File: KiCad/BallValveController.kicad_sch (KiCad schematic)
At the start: 53 parts, among them J1 Screw_Terminal_01x03, J2 Screw_Terminal_01x04, J3 Screw_Terminal_01x04, J4 Screw_Terminal_01x04, J5 Conn_01x01_Male, J6 Screw_Terminal_01x04, J7 Screw_Terminal_01x02, K1 G5V-2, Q1 Q_PMOS_GDS, Q2 2N2222A, U1 MT2499A, U2 L7805, U3 XIAO-ESP32-C6

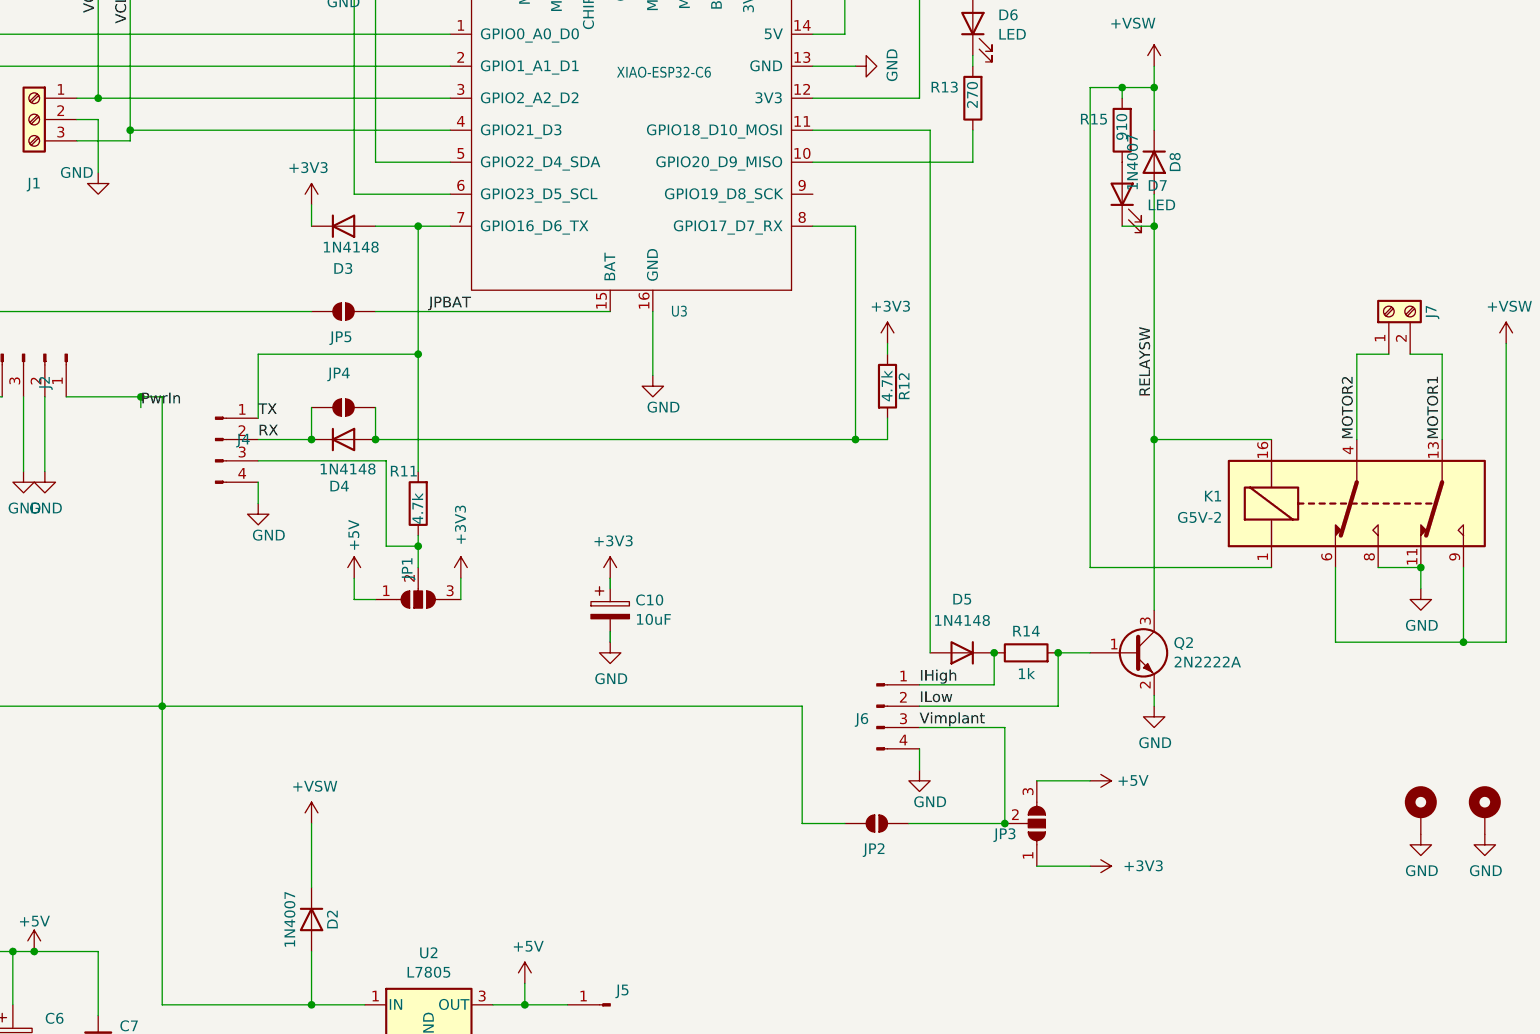
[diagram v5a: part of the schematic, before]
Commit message: New layout - changed Diodes and Cap footprints + RX/TX wiring
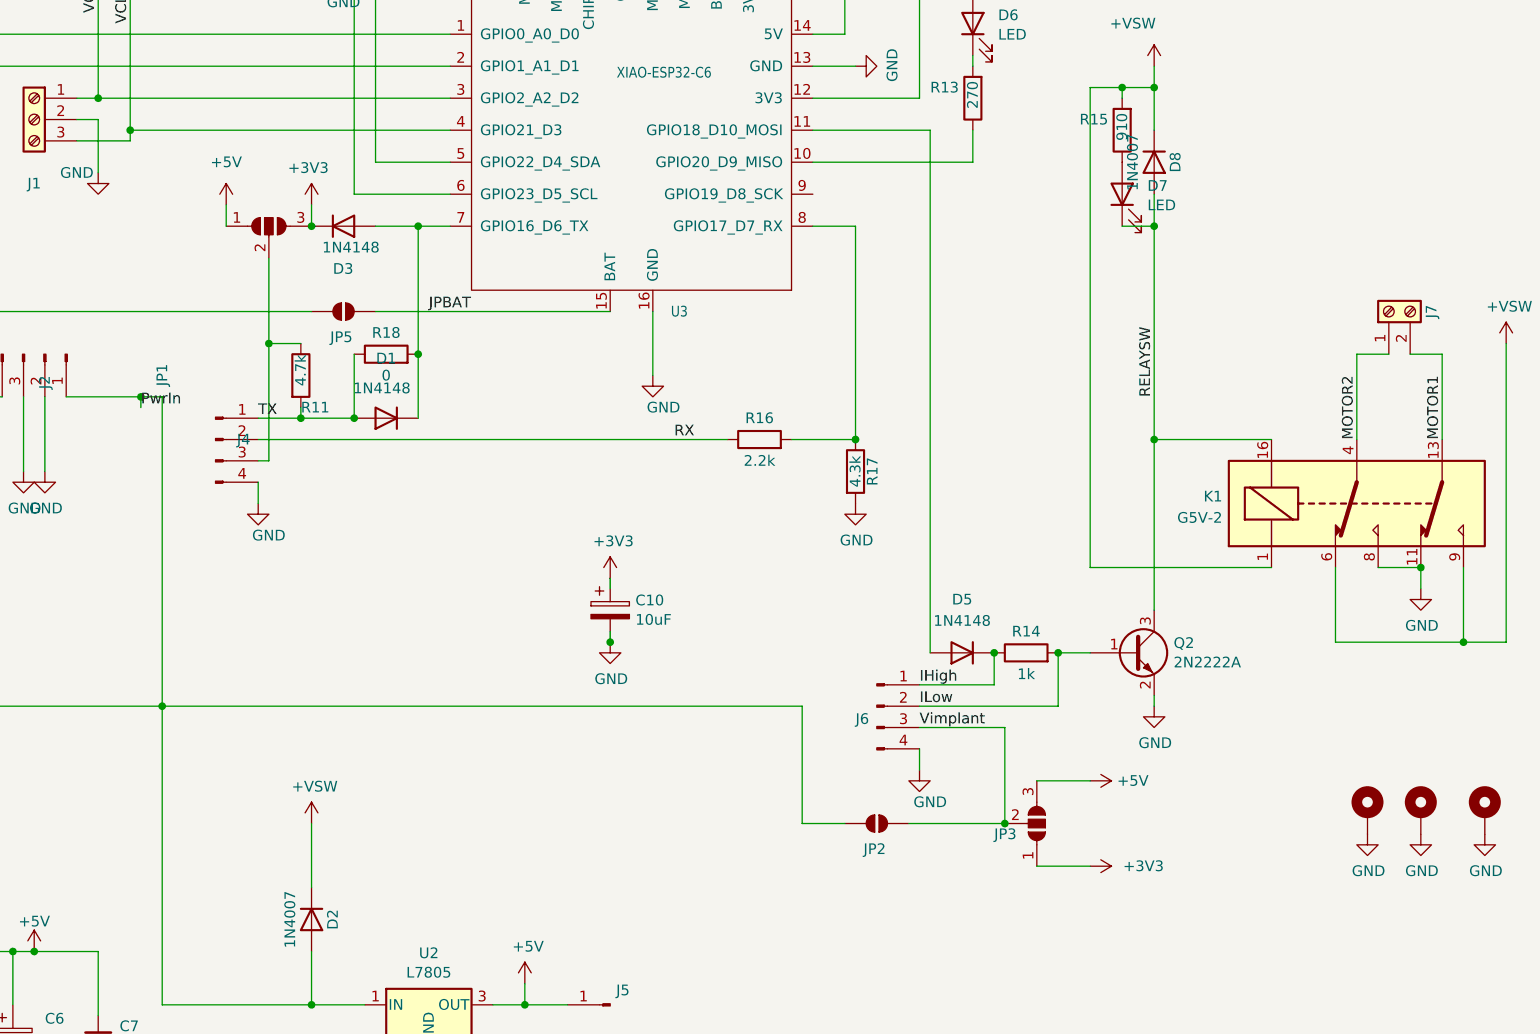
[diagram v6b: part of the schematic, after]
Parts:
- removed D4: 1N4148, Diode_SMD:D_SOD-323_HandSoldering, symbol Device:D
- removed JP4: SolderJumper_2_Open, Jumper:SolderJumper-2_P1.3mm_Open_RoundedPad1.0x1.5mm, symbol Jumper:SolderJumper_2_Open
- removed R12: 4.7k, Resistor_SMD:R_0805_2012Metric_Pad1.20x1.40mm_HandSolder, symbol Device:R
- added D1: 1N4148, Diode_SMD:D_SOD-323_HandSoldering, symbol Device:D
- added H2: MountingHole_Pad, MountingHole:MountingHole_3.2mm_M3_ISO14580_Pad, symbol Mechanical:MountingHole_Pad
- added R16: 2.2k, Resistor_SMD:R_0805_2012Metric_Pad1.20x1.40mm_HandSolder, symbol Device:R
- added R17: 4.3k, Resistor_SMD:R_0805_2012Metric_Pad1.20x1.40mm_HandSolder, symbol Device:R
- added R18: 0, Resistor_SMD:R_0805_2012Metric_Pad1.20x1.40mm_HandSolder, symbol Device:R
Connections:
- net GND: now also H2.1, R17.2
- net RX: now also R16.1
- net TX: now also D1.2 (A), R18.1; no longer D3.2 (A), U3.7 (GPIO16_D6_TX)
- net at U3.8 (GPIO17_D7_RX): now also R16.2, R17.1
- new net: D1.1 (K), D3.2 (A), R18.2, U3.7 (GPIO16_D6_TX)
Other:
- moved on the sheet: JP1, R11

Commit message: Version 8.0.2 pdf files
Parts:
- added TP1, TP2, TP3, TP4, TP5, TP6: TestPoint, TestPoint:TestPoint_THTPad_D1.0mm_Drill0.5mm, symbol Connector:TestPoint
- Q2: footprint Package_TO_SOT_SMD:SOT-23_Handsoldering -> Package_TO_SOT_SMD:SOT-23
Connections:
- net +3V3: now also TP3.1
- net +5V: now also TP2.1
- net +VSW: now also TP5.1
- net RELAYSW: now also TP4.1
- net VBAT: now also TP6.1
- net at C4.2, Q1.1 (G), R6.1: now also TP1.1
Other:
- title: Ball Valve Controller for CR05-02 wiring - ESP32-C3 version -> Ball Valve Controller for CR05-02 wiring - ESP32-C3/C6

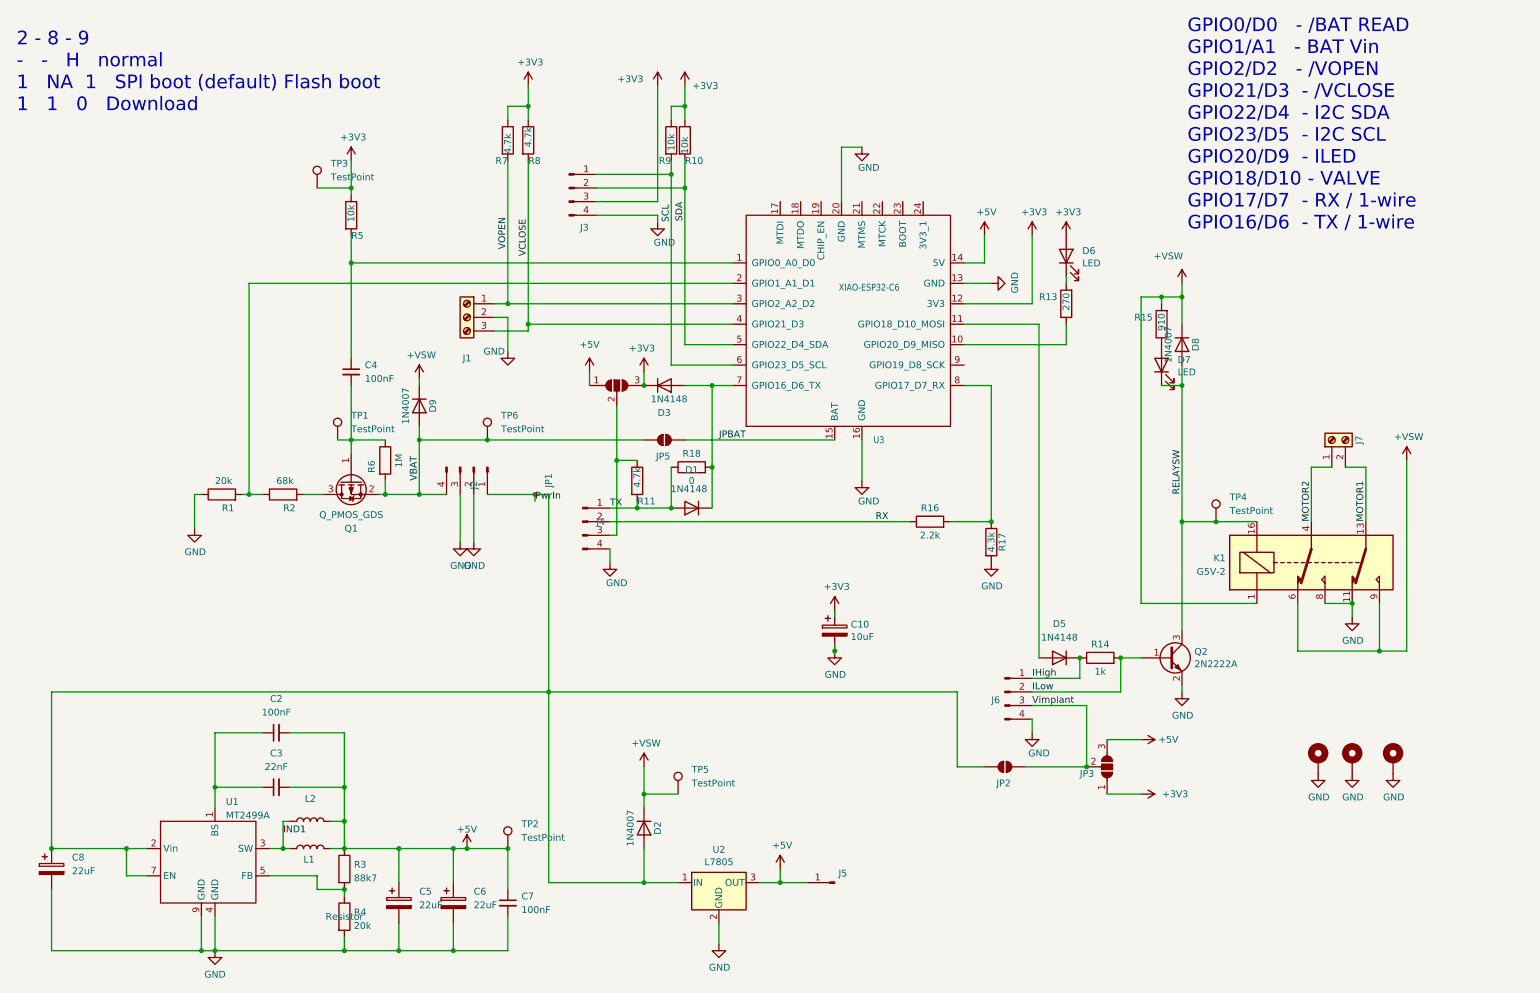
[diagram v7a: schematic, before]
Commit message: Fixed MT2499A layout
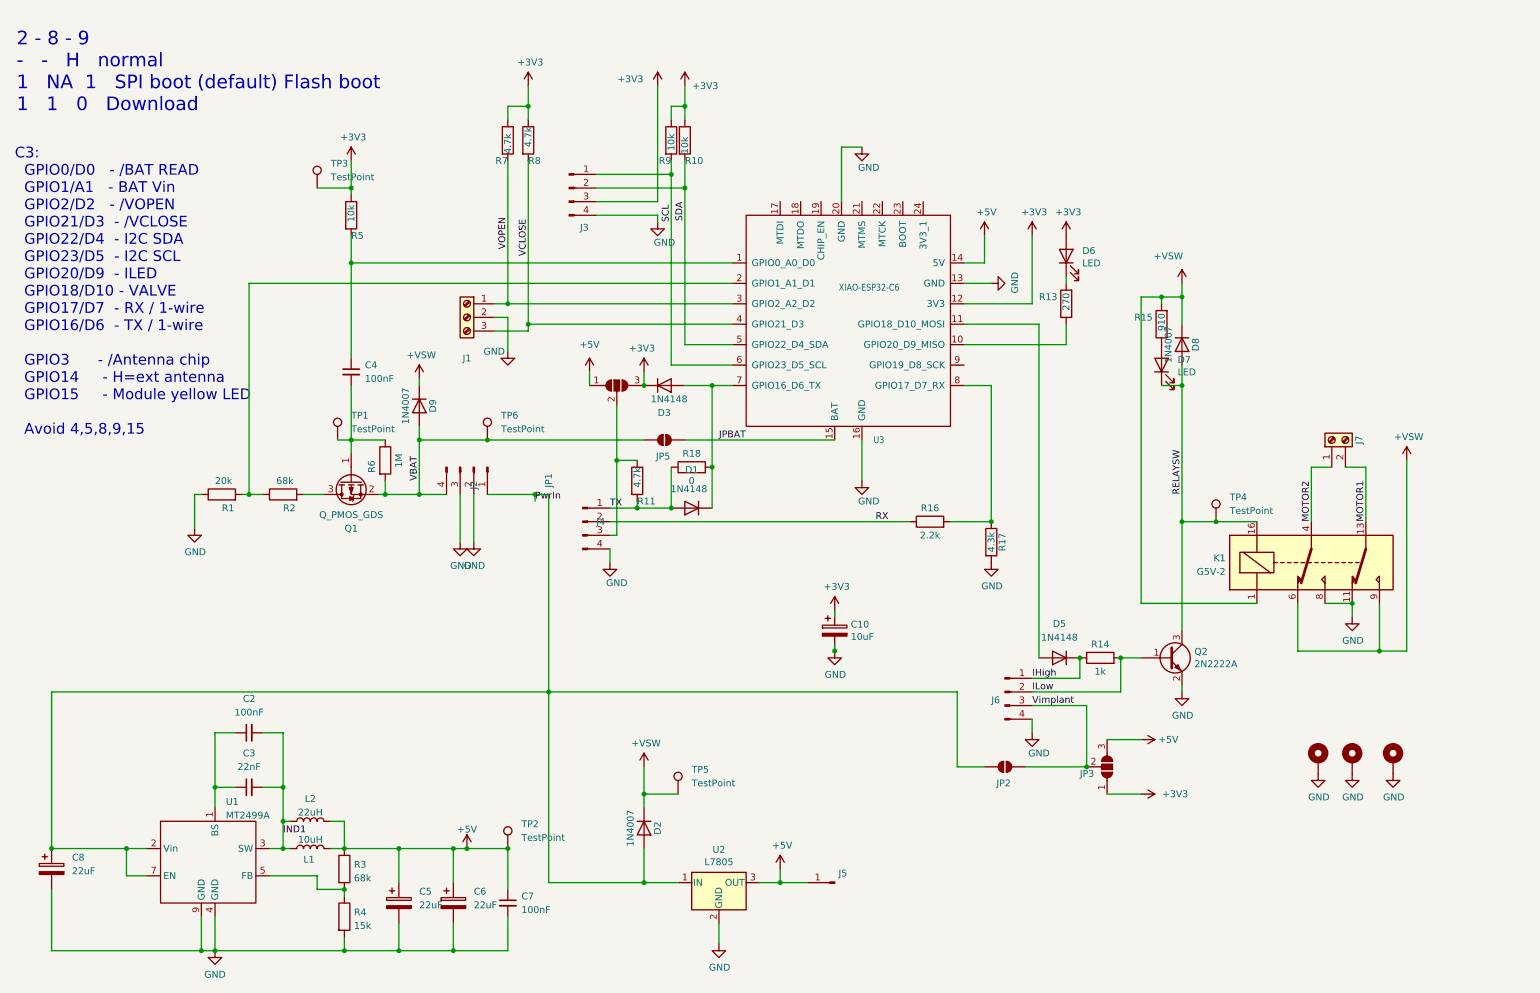
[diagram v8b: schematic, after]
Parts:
- L1: value L -> 10uH; footprint Inductor_SMD:L_2512_6332Metric_Pad1.52x3.35mm_HandSolder -> Inductor_SMD:L_2010_5025Metric_Pad1.52x2.65mm_HandSolder
- L2: value L -> 22uH
- R3: value 88k7 -> 68k
- R4: value 20k -> 15k
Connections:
- net +5V: no longer C2.2, C3.2
- net IND1: now also C2.2, C3.2
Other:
- note added: "C3: GPIO0/D0 - /BAT READ GPIO1/A1 - BAT Vin GPIO2/D2 - /VOPEN GPIO21/D3 - /VCLOSE GPIO22/D4 - I2C SDA GPIO23/D5 - I2C SCL GPIO20/D9 - ILED GPIO18/D10 - VALVE GPIO17/D7 - RX / 1-wire GPIO16/D6 - TX / 1-wire GPIO3 - /Antenna chip GPIO14 - H=ext antenna GPIO15 - Module yellow LED Avoid 4,5,8,9,15"
- note removed: "GPIO0/D0 - /BAT READ GPIO1/A1 - BAT Vin GPIO2/D2 - /VOPEN GPIO21/D3 - /VCLOSE GPIO22/D4 - I2C SDA GPIO23/D5 - I2C SCL GPIO20/D9 - ILED GPIO18/D10 - VALVE GPIO17/D7 - RX / 1-wire GPIO16/D6 - TX / 1-wire"
- moved on the sheet: C2, C3
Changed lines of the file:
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@@
 		)
 	)
-	(text "GPIO0/D0   - /BAT READ\nGPIO1/A1   - BAT Vin\nGPIO2/D2   - /VOPEN\nGPIO21/D3  - /VCLOSE\nGPIO22/D4  - I2C SDA\nGPIO23/D5  - I2C SCL\nGPIO20/D9  - ILED\nGPIO18/D10 - VALVE\nGPIO17/D7  - RX / 1-wire\nGPIO16/D6  - TX / 1-wire\n\n"
+	(text "C3:\n  GPIO0/D0   - /BAT READ\n  GPIO1/A1   - BAT Vin\n  GPIO2/D2   - /VOPEN\n  GPIO21/D3  - /VCLOSE\n  GPIO22/D4  - I2C SDA\n  GPIO23/D5  - I2C SCL\n  GPIO20/D9  - ILED\n  GPIO18/D10 - VALVE\n  GPIO17/D7  - RX / 1-wire\n  GPIO16/D6  - TX / 1-wire\n\n  GPIO3      - /Antenna chip\n  GPIO14     - H=ext antenna\n  GPIO15     - Module yellow LED\n\n  Avoid 4,5,8,9,15\n\n"
 		(exclude_from_sim no)
-		(at 233.426 59.182 0)
+		(at 14.732 96.52 0)
 		(effects
 			(font
 				(face "Andale Mono")
-				(size 2.54 2.54)
+				(size 2 2)
 			)
 			(justify left bottom)
@@
 	)
 	(junction
-		(at 232.41 109.22)
+		(at 64.77 165.1)
 		(diameter 0)
 		(color 0 0 0 0)
 	)
 	(junction
-		(at 111.76 104.14)
+		(at 232.41 109.22)
 		(diameter 0)
 		(color 0 0 0 0)
 	)
 	(junction
-		(at 213.36 134.62)
+		(at 111.76 104.14)
 		(diameter 0)
 		(color 0 0 0 0)
 	)
 	(junction
-		(at 232.41 67.31)
+		(at 213.36 134.62)
 		(diameter 0)
 		(color 0 0 0 0)
 	)
 	(junction
-		(at 76.2 158.75)
+		(at 232.41 67.31)
 		(diameter 0)
 		(color 0 0 0 0)
@@
 	)
 	(junction
+		(at 64.77 158.75)
+		(diameter 0)
+		(color 0 0 0 0)
+	)
+	(junction
 		(at 76.2 177.8)
 		(diameter 0)
@@
 	)
 	(junction
-		(at 76.2 165.1)
-		(diameter 0)
-		(color 0 0 0 0)
-	)
-	(junction
 		(at 58.42 104.14)
 		(diameter 0)
@@
 	(wire
 		(pts
-			(xy 52.07 148.59) (xy 60.96 148.59)
+			(xy 52.07 148.59) (xy 55.88 148.59)
 		)
 		(stroke
@@
 	(wire
 		(pts
-			(xy 66.04 148.59) (xy 76.2 148.59)
+			(xy 60.96 148.59) (xy 64.77 148.59)
 		)
 		(stroke
@@
 	(wire
 		(pts
-			(xy 52.07 158.75) (xy 60.96 158.75)
+			(xy 52.07 158.75) (xy 55.88 158.75)
 		)
 		(stroke
@@
 	(wire
 		(pts
-			(xy 66.04 158.75) (xy 76.2 158.75)
+			(xy 60.96 158.75) (xy 64.77 158.75)
 		)
 		(stroke
@@
 	(wire
 		(pts
-			(xy 76.2 148.59) (xy 76.2 158.75)
+			(xy 64.77 148.59) (xy 64.77 158.75)
 		)
 		(stroke
@@
 	(wire
 		(pts
-			(xy 76.2 158.75) (xy 76.2 165.1)
-		)
-		(stroke
-			(width 0)
-			(type default)
-		)
-	)
-	(wire
-		(pts
 			(xy 220.98 134.62) (xy 220.98 140.97)
 		)
@@
 	(wire
 		(pts
+			(xy 64.77 158.75) (xy 64.77 165.1)
+		)
+		(stroke
+			(width 0)
+			(type default)
+		)
+	)
+	(wire
+		(pts
 			(xy 123.19 44.45) (xy 137.16 44.45)
 		)
@@
 			)
 		)
-		(property "Value" "20k"
+		(property "Value" "15k"
 			(at 77.978 184.5822 0)
 			(effects
@@
 					(size 1.27 1.27)
 				)
+				(hide yes)
 			)
 		)
@@
 			)
 		)
-		(property "Value" "88k7"
+		(property "Value" "68k"
 			(at 77.978 175.6922 0)
 			(effects
@@
 			)
 		)
-		(property "Value" "L"
+		(property "Value" "10uH"
 			(at 69.85 168.5091 90)
 			(effects
@@
 					(size 1.27 1.27)
 				)
-				(hide yes)
 			)
 		)
-		(property "Footprint" "Inductor_SMD:L_2512_6332Metric_Pad1.52x3.35mm_HandSolder"
+		(property "Footprint" "Inductor_SMD:L_2010_5025Metric_Pad1.52x2.65mm_HandSolder"
 			(at 69.85 170.18 0)
 			(effects
@@
 	(symbol
 		(lib_id "Device:C_Small")
-		(at 63.5 148.59 90)
+		(at 58.42 148.59 90)
 		(unit 1)
 		(exclude_from_sim no)
@@
 		(fields_autoplaced yes)
 		(property "Reference" "C2"
-			(at 63.5063 142.24 90)
+			(at 58.4263 142.24 90)
 			(effects
 				(font
@@
 		)
 		(property "Value" "100nF"
-			(at 63.5063 144.78 90)
+			(at 58.4263 144.78 90)
 			(effects
 				(font
@@
 		)
 		(property "Footprint" "Capacitor_SMD:C_0805_2012Metric_Pad1.18x1.45mm_HandSolder"
-			(at 63.5 148.59 0)
+			(at 58.42 148.59 0)
 			(effects
 				(font
@@
 		)
 		(property "Datasheet" "~"
-			(at 63.5 148.59 0)
+			(at 58.42 148.59 0)
 			(effects
 				(font
@@
 		)
 		(property "Description" "Unpolarized capacitor, small symbol"
-			(at 63.5 148.59 0)
+			(at 58.42 148.59 0)
 			(effects
 				(font
@@
 			)
 		)
-		(property "Value" "L"
+		(property "Value" "22uH"
 			(at 69.85 163.4291 90)
 			(effects
@@
 					(size 1.27 1.27)
 				)
-				(hide yes)
 			)
 		)
@@
 	(symbol
 		(lib_id "Device:C_Small")
-		(at 63.5 158.75 90)
+		(at 58.42 158.75 90)
 		(unit 1)
 		(exclude_from_sim no)
@@
 		(fields_autoplaced yes)
 		(property "Reference" "C3"
-			(at 63.5063 152.4 90)
+			(at 58.4263 152.4 90)
 			(effects
 				(font
@@
 		)
 		(property "Value" "22nF"
-			(at 63.5063 154.94 90)
+			(at 58.4263 154.94 90)
 			(effects
 				(font
@@
 		)
 		(property "Footprint" "Capacitor_SMD:C_0805_2012Metric_Pad1.18x1.45mm_HandSolder"
-			(at 63.5 158.75 0)
+			(at 58.42 158.75 0)
 			(effects
 				(font
@@
 		)
 		(property "Datasheet" "~"
-			(at 63.5 158.75 0)
+			(at 58.42 158.75 0)
 			(effects
 				(font
@@
 		)
 		(property "Description" "Unpolarized capacitor, small symbol"
-			(at 63.5 158.75 0)
+			(at 58.42 158.75 0)
 			(effects
 				(font
@@
 		)
 		(property "JLCPCB Part#" "C1729"
-			(at 63.5 158.75 90)
+			(at 58.42 158.75 90)
 			(effects
 				(font
